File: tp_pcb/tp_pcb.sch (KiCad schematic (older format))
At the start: 22 parts, among them K0 KEYSW, K1 KEYSW, K2 KEYSW, K3 KEYSW, K4 KEYSW, K5 KEYSW, K6 KEYSW, P0 CONN_01X08, P1 CONN_01X08, P2 CONN_01X06

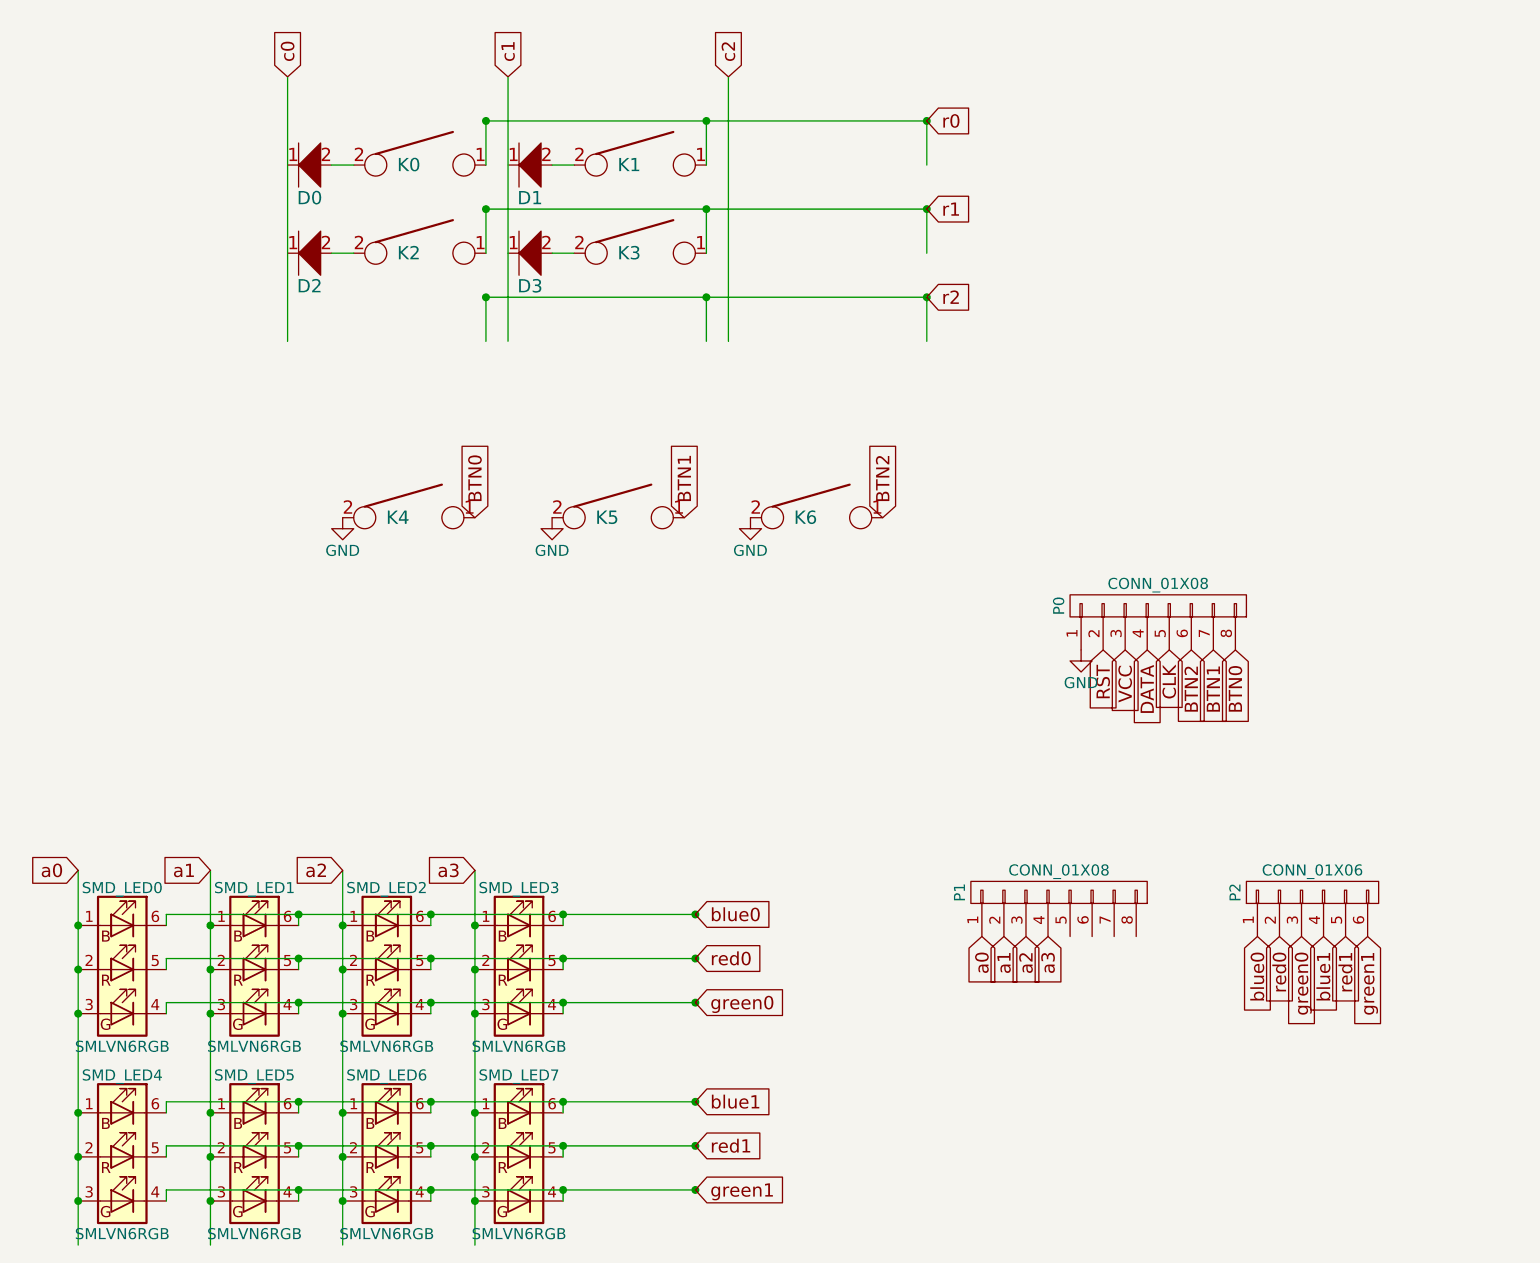
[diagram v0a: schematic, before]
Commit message: tp_pcb routing, woo interactive
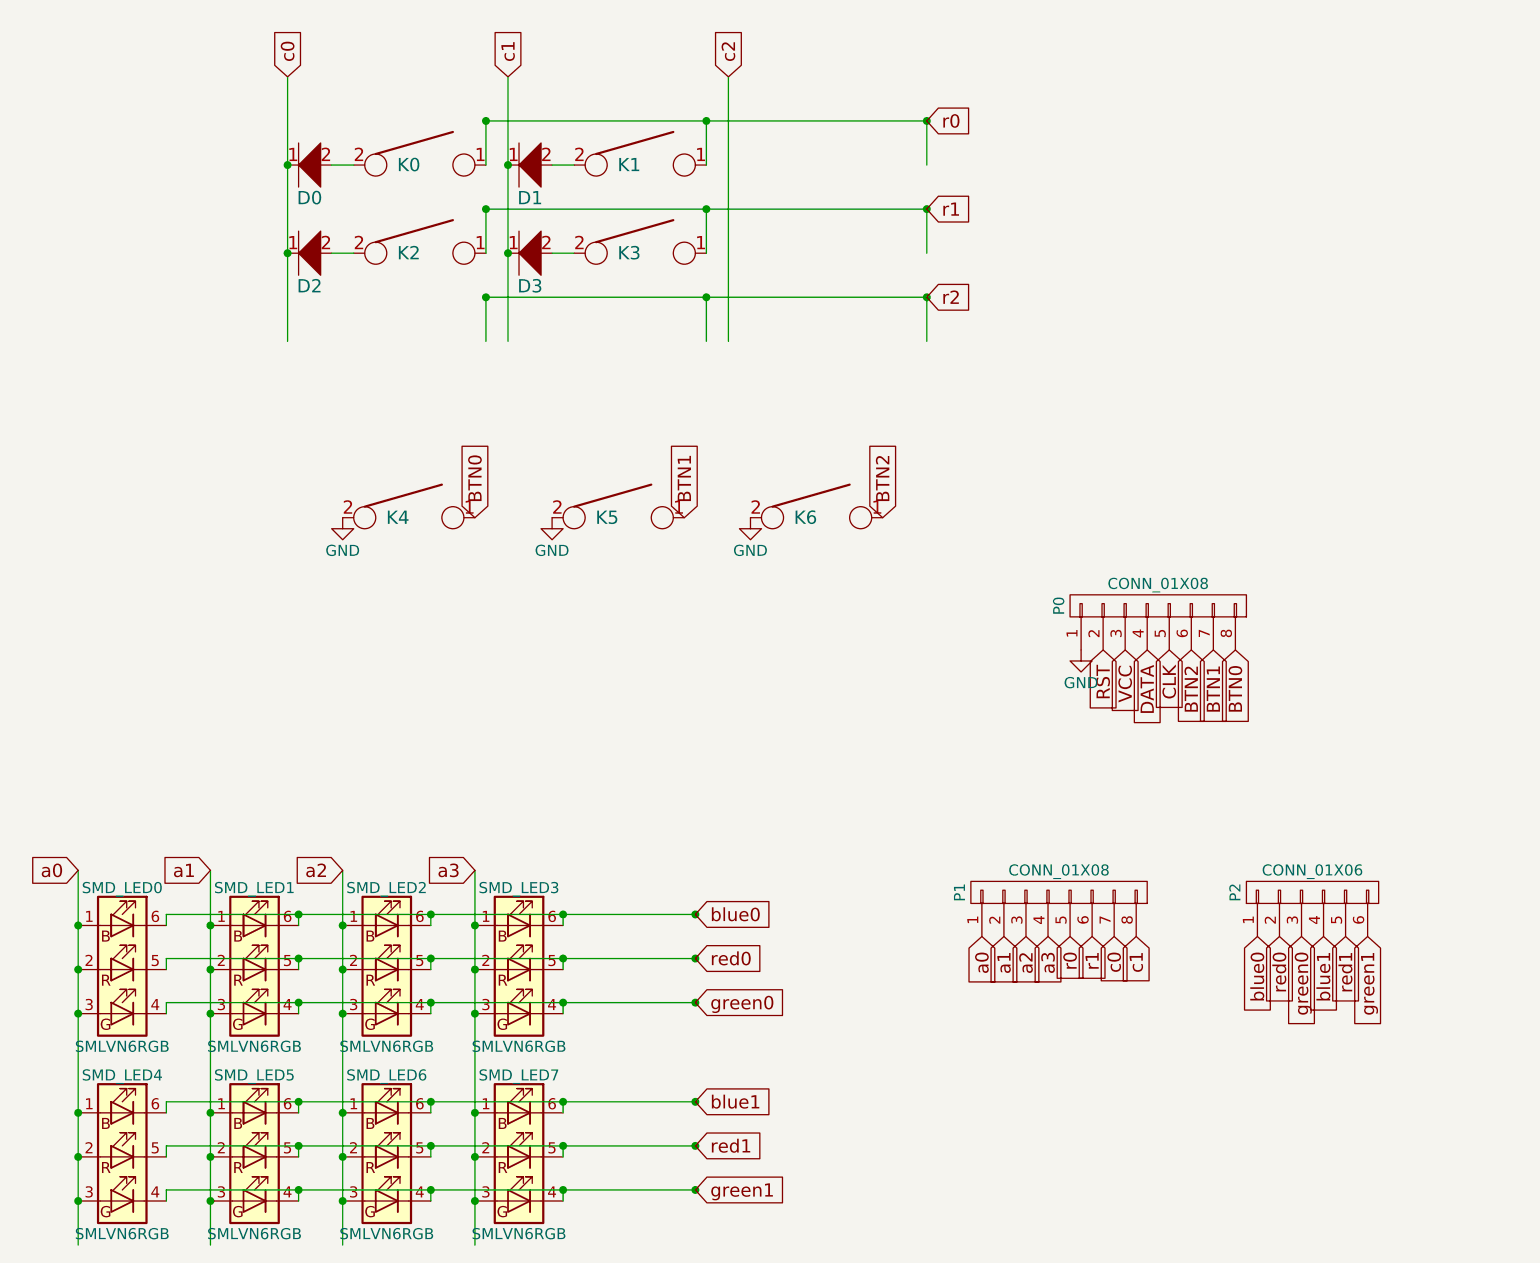
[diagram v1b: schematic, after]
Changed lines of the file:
@@
 LIBS:contrib
 LIBS:valves
+LIBS:tp_pcb-cache
 EELAYER 25 0
 EELAYER END
@@
 $EndComp
 $Comp
-L GND #PWR1
+L GND #PWR01
 U 1 1 58AC27C9
 P 3950 3800
-F 0 "#PWR1" H 3950 3550 50  0001 C CNN
+F 0 "#PWR01" H 3950 3550 50  0001 C CNN
 F 1 "GND" H 3950 3650 50  0000 C CNN
 F 2 "" H 3950 3800 50  0000 C CNN
@@
 $EndComp
 $Comp
-L GND #PWR2
+L GND #PWR02
 U 1 1 58AC28A0
 P 4900 3800
-F 0 "#PWR2" H 4900 3550 50  0001 C CNN
+F 0 "#PWR02" H 4900 3550 50  0001 C CNN
 F 1 "GND" H 4900 3650 50  0000 C CNN
 F 2 "" H 4900 3800 50  0000 C CNN
@@
 $EndComp
 $Comp
-L GND #PWR3
+L GND #PWR03
 U 1 1 58AC28D2
 P 5800 3800
-F 0 "#PWR3" H 5800 3550 50  0001 C CNN
+F 0 "#PWR03" H 5800 3550 50  0001 C CNN
 F 1 "GND" H 5800 3650 50  0000 C CNN
 F 2 "" H 5800 3800 50  0000 C CNN
@@
 $EndComp
 $Comp
-L GND #PWR4
+L GND #PWR04
 U 1 1 58AC2904
 P 7300 4400
-F 0 "#PWR4" H 7300 4150 50  0001 C CNN
+F 0 "#PWR04" H 7300 4150 50  0001 C CNN
 F 1 "GND" H 7300 4250 50  0000 C CNN
 F 2 "" H 7300 4400 50  0000 C CNN
@@
 	6600 2400 6600 2600
 Wire Wire Line
-	4950 5650 4950 5600
+	4950 5600 4950 5650
 Wire Wire Line
 	3150 5600 5550 5600
 Wire Wire Line
-	4950 5850 4950 5800
+	4950 5800 4950 5850
 Wire Wire Line
 	3150 5800 5550 5800
 Wire Wire Line
-	4950 6050 4950 6000
+	4950 6000 4950 6050
 Wire Wire Line
 	3150 6000 5550 6000
@@
 Text GLabel 7400 4400 3    60   Input ~ 0
 RST
+Text GLabel 7250 5700 3    60   Input ~ 0
+r0
+Text GLabel 7350 5700 3    60   Input ~ 0
+r1
+Text GLabel 7450 5700 3    60   Input ~ 0
+c0
+Text GLabel 7550 5700 3    60   Input ~ 0
+c1
+Connection ~ 4700 2600
+Connection ~ 4700 2200
+Connection ~ 3700 2200
+Connection ~ 3700 2600
 $EndSCHEMATC

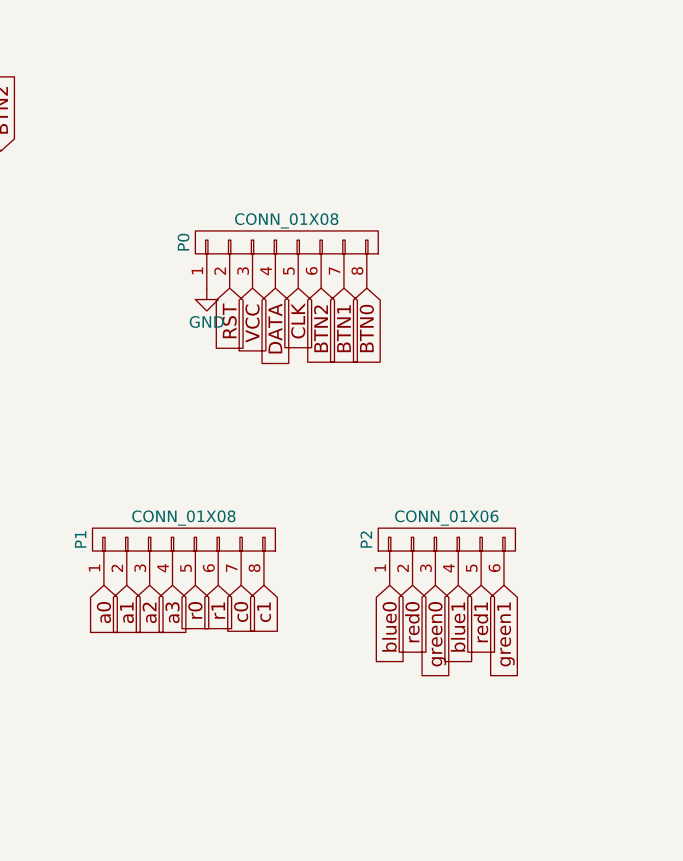
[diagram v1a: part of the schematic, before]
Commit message: tp major improvements + routing, tp holes improved and modified
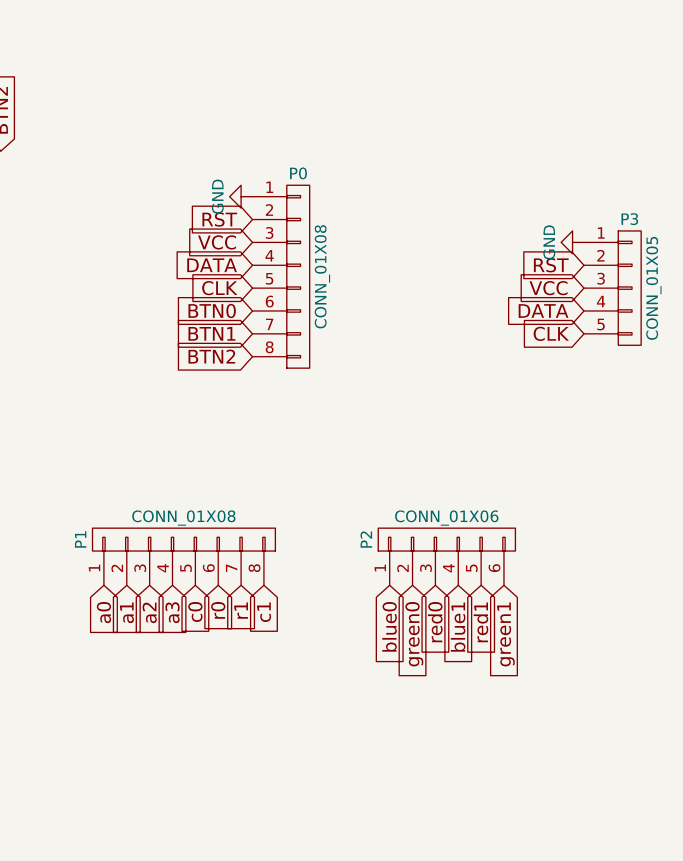
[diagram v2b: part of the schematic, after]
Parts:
- added P3: CONN_01X05, Socket_Strips:Socket_Strip_Straight_1x05_Pitch2.54mm, symbol CONN_01X05
- SMD_LED0, SMD_LED1, SMD_LED2, SMD_LED3, SMD_LED4, SMD_LED5, SMD_LED6, SMD_LED7: footprint cherry_rgb:SMLVN6RGB -> cherry_rgb:SMLVN6RGB_CA
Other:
- moved on the sheet: P0
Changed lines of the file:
@@
 L CONN_01X08 P0
 U 1 1 58ABFDEF
-P 7650 4200
-F 0 "P0" H 7650 4650 50  0000 C CNN
-F 1 "CONN_01X08" V 7750 4200 50  0000 C CNN
-F 2 "Connectors_Molex:Molex_PicoBlade_53261-0871_08x1.25mm_Angled" H 7650 4200 50  0001 C CNN
-F 3 "" H 7650 4200 50  0000 C CNN
-	1    7650 4200
-	0    -1   -1   0
+P 7700 4350
+F 0 "P0" H 7700 4800 50  0000 C CNN
+F 1 "CONN_01X08" V 7800 4350 50  0000 C CNN
+F 2 "Connectors_Molex:Molex_PicoBlade_53261-0871_08x1.25mm_Angled" H 7700 4350 50  0001 C CNN
+F 3 "" H 7700 4350 50  0000 C CNN
+	1    7700 4350
+	1    0    0    -1
 $EndComp
 $Comp
@@
 L GND #PWR04
 U 1 1 58AC2904
-P 7300 4400
-F 0 "#PWR04" H 7300 4150 50  0001 C CNN
-F 1 "GND" H 7300 4250 50  0000 C CNN
-F 2 "" H 7300 4400 50  0000 C CNN
-F 3 "" H 7300 4400 50  0000 C CNN
-	1    7300 4400
-	1    0    0    -1
+P 7500 4000
+F 0 "#PWR04" H 7500 3750 50  0001 C CNN
+F 1 "GND" H 7500 3850 50  0000 C CNN
+F 2 "" H 7500 4000 50  0000 C CNN
+F 3 "" H 7500 4000 50  0000 C CNN
+	1    7500 4000
+	0    1    1    0
 $EndComp
 Text GLabel 4550 3800 1    60   Input ~ 0
@@
 Text GLabel 6400 3800 1    60   Input ~ 0
 BTN2
-Text GLabel 8000 4400 3    60   Input ~ 0
+Text GLabel 7500 4500 0    60   Input ~ 0
 BTN0
-Text GLabel 7900 4400 3    60   Input ~ 0
+Text GLabel 7500 4600 0    60   Input ~ 0
 BTN1
-Text GLabel 7800 4400 3    60   Input ~ 0
+Text GLabel 7500 4700 0    60   Input ~ 0
 BTN2
 Wire Wire Line
@@
 F 0 "SMD_LED0" H 2950 6220 50  0000 C CNN
 F 1 "SMLVN6RGB" H 2950 5500 50  0000 C CNN
-F 2 "cherry_rgb:SMLVN6RGB" H 2950 5800 50  0001 C CNN
+F 2 "cherry_rgb:SMLVN6RGB_CA" H 2950 5800 50  0001 C CNN
 F 3 "" H 2950 5800 50  0000 C CNN
 	1    2950 5850
@@
 F 0 "SMD_LED1" H 3550 6220 50  0000 C CNN
 F 1 "SMLVN6RGB" H 3550 5500 50  0000 C CNN
-F 2 "cherry_rgb:SMLVN6RGB" H 3550 5800 50  0001 C CNN
+F 2 "cherry_rgb:SMLVN6RGB_CA" H 3550 5800 50  0001 C CNN
 F 3 "" H 3550 5800 50  0000 C CNN
 	1    3550 5850
@@
 F 0 "SMD_LED2" H 4150 6220 50  0000 C CNN
 F 1 "SMLVN6RGB" H 4150 5500 50  0000 C CNN
-F 2 "cherry_rgb:SMLVN6RGB" H 4150 5800 50  0001 C CNN
+F 2 "cherry_rgb:SMLVN6RGB_CA" H 4150 5800 50  0001 C CNN
 F 3 "" H 4150 5800 50  0000 C CNN
 	1    4150 5850
@@
 F 0 "SMD_LED3" H 4750 6220 50  0000 C CNN
 F 1 "SMLVN6RGB" H 4750 5500 50  0000 C CNN
-F 2 "cherry_rgb:SMLVN6RGB" H 4750 5800 50  0001 C CNN
+F 2 "cherry_rgb:SMLVN6RGB_CA" H 4750 5800 50  0001 C CNN
 F 3 "" H 4750 5800 50  0000 C CNN
 	1    4750 5850
@@
 F 0 "SMD_LED4" H 2950 7070 50  0000 C CNN
 F 1 "SMLVN6RGB" H 2950 6350 50  0000 C CNN
-F 2 "cherry_rgb:SMLVN6RGB" H 2950 6650 50  0001 C CNN
+F 2 "cherry_rgb:SMLVN6RGB_CA" H 2950 6650 50  0001 C CNN
 F 3 "" H 2950 6650 50  0000 C CNN
 	1    2950 6700
@@
 F 0 "SMD_LED5" H 3550 7070 50  0000 C CNN
 F 1 "SMLVN6RGB" H 3550 6350 50  0000 C CNN
-F 2 "cherry_rgb:SMLVN6RGB" H 3550 6650 50  0001 C CNN
+F 2 "cherry_rgb:SMLVN6RGB_CA" H 3550 6650 50  0001 C CNN
 F 3 "" H 3550 6650 50  0000 C CNN
 	1    3550 6700
@@
 F 0 "SMD_LED6" H 4150 7070 50  0000 C CNN
 F 1 "SMLVN6RGB" H 4150 6350 50  0000 C CNN
-F 2 "cherry_rgb:SMLVN6RGB" H 4150 6650 50  0001 C CNN
+F 2 "cherry_rgb:SMLVN6RGB_CA" H 4150 6650 50  0001 C CNN
 F 3 "" H 4150 6650 50  0000 C CNN
 	1    4150 6700
@@
 F 0 "SMD_LED7" H 4750 7070 50  0000 C CNN
 F 1 "SMLVN6RGB" H 4750 6350 50  0000 C CNN
-F 2 "cherry_rgb:SMLVN6RGB" H 4750 6650 50  0001 C CNN
+F 2 "cherry_rgb:SMLVN6RGB_CA" H 4750 6650 50  0001 C CNN
 F 3 "" H 4750 6650 50  0000 C CNN
 	1    4750 6700
@@
 	0    -1   -1   0
 $EndComp
+Text GLabel 8300 5700 3    60   Input ~ 0
+red0
 Text GLabel 8200 5700 3    60   Input ~ 0
-red0
-Text GLabel 8300 5700 3    60   Input ~ 0
 green0
 Text GLabel 8100 5700 3    60   Input ~ 0
@@
 Text GLabel 7150 5700 3    60   Input ~ 0
 a3
-Text GLabel 7700 4400 3    60   Input ~ 0
+Text GLabel 7500 4400 0    60   Input ~ 0
 CLK
-Text GLabel 7600 4400 3    60   Input ~ 0
+Text GLabel 7500 4300 0    60   Input ~ 0
 DATA
-Text GLabel 7500 4400 3    60   Input ~ 0
+Text GLabel 7500 4200 0    60   Input ~ 0
 VCC
-Text GLabel 7400 4400 3    60   Input ~ 0
+Text GLabel 7500 4100 0    60   Input ~ 0
 RST
+Text GLabel 7350 5700 3    60   Input ~ 0
+r0
+Text GLabel 7450 5700 3    60   Input ~ 0
+r1
 Text GLabel 7250 5700 3    60   Input ~ 0
-r0
-Text GLabel 7350 5700 3    60   Input ~ 0
-r1
-Text GLabel 7450 5700 3    60   Input ~ 0
 c0
 Text GLabel 7550 5700 3    60   Input ~ 0
@@
 Connection ~ 3700 2200
 Connection ~ 3700 2600
+Text GLabel 8950 4600 0    60   Input ~ 0
+CLK
+Text GLabel 8950 4500 0    60   Input ~ 0
+DATA
+Text GLabel 8950 4400 0    60   Input ~ 0
+VCC
+Text GLabel 8950 4300 0    60   Input ~ 0
+RST
+$Comp
+L GND #PWR05
+U 1 1 58B2C683
+P 8950 4200
+F 0 "#PWR05" H 8950 3950 50  0001 C CNN
+F 1 "GND" H 8950 4050 50  0000 C CNN
+F 2 "" H 8950 4200 50  0000 C CNN
+F 3 "" H 8950 4200 50  0000 C CNN
+	1    8950 4200
+	0    1    1    0
+$EndComp
+$Comp
+L CONN_01X05 P3
+U 1 1 58B2CB75
+P 9150 4400
+F 0 "P3" H 9150 4700 50  0000 C CNN
+F 1 "CONN_01X05" V 9250 4400 50  0000 C CNN
+F 2 "Socket_Strips:Socket_Strip_Straight_1x05_Pitch2.54mm" H 9150 4400 50  0001 C CNN
+F 3 "" H 9150 4400 50  0000 C CNN
+	1    9150 4400
+	1    0    0    -1
+$EndComp
 $EndSCHEMATC
